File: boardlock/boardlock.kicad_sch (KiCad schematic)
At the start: 15 parts, among them SW1 SW_Push, SW2 SW_Push, U1 ESP32-S3-WROOM-1

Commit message: buttons and stuff
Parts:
- removed C23, C24: 0.1uF, symbol Device:C_Small
- removed D2: CLVBA-FKA-CC1F1L1BB7R3R3D, symbol Device:LED_RABG
- removed R18: 175, symbol Device:R_Small_US
- removed R19, R20: 40, symbol Device:R_Small_US
- removed R21, R22: 10k, symbol Device:R_Small_US
- removed SW1, SW2: SW_Push, symbol Switch:SW_Push
- added TP29, TP30: TestPoint, symbol Connector:TestPoint
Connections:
- net at U1.31 (GPIO38/FSPIWP/SUBSPIWP): now also TP30.1
- net M_BUTTON_INT: now reaches U1.38 (GPIO2/TOUCH2/ADC1_CH1)
- net M_BUTTON_EXT: now reaches U1.39 (GPIO1/TOUCH1/ADC1_CH0)
- net at U1.4 (GPIO4/TOUCH4/ADC1_CH3): now also TP29.1
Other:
- note removed: "assuming using big LED, change pin order if not"
- note removed: "check other circuitry in dev kit schematic"
- note removed: "maybe 100k"
- note removed: "uC dev kit has 2 caps"

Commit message: lab updates
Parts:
- removed TP29, TP30: TestPoint, symbol Connector:TestPoint
- added D3: LED, symbol Device:LED
- added R29: R_US, symbol Device:R_US
- added TP31: TX (backup programming), symbol Connector:TestPoint
- added TP32: RX (backup programming), symbol Connector:TestPoint
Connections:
- net GND: now also D3.1 (K)
- net M_I2S_BCLK: now also U1.24 (GPIO47/SPICLK_P/SUBSPICLK_P_DIFF); no longer U1.8 (GPIO15/U0RTS/ADC2_CH4/XTAL_32K_P)
- net M_I2S_Data_Out: now also U1.26 (GPIO45); no longer U1.22 (GPIO14/TOUCH14/ADC2_CH3/FSPIWP/FSPIDQS/SUBSPIWP)
- net M_I2S_LRC: now also U1.25 (GPIO48/SPICLK_N/SUBSPICLK_N_DIFF); no longer U1.9 (GPIO16/U0CTS/ADC2_CH5/XTAL_32K_N)
- net M_BUTTON_EXT2: now reaches U1.4 (GPIO4/TOUCH4/ADC1_CH3)
- net at U1.36 (U0RXD/GPIO44/CLK_OUT2): now also TP32.1
- net at U1.37 (U0TXD/GPIO43/CLK_OUT1): now also TP31.1
- net M_BUTTON_EXT renamed M_BUTTON_EXT1
- new net: D3.2 (A), R29.2
- new net M_HEARTBEAT: R29.1
- no-connect marks 0 -> 3
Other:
- note added: "35: input only"
- note added: "36: input only"
- note added: "37: input only"
- note added: "38: input only"
- note added: "39: input only"
- note added: "Arrange RGB, I2S, and buttons such that the pins are close to their respective function"
- note added: "figure out what pins can actually be used for stuff"

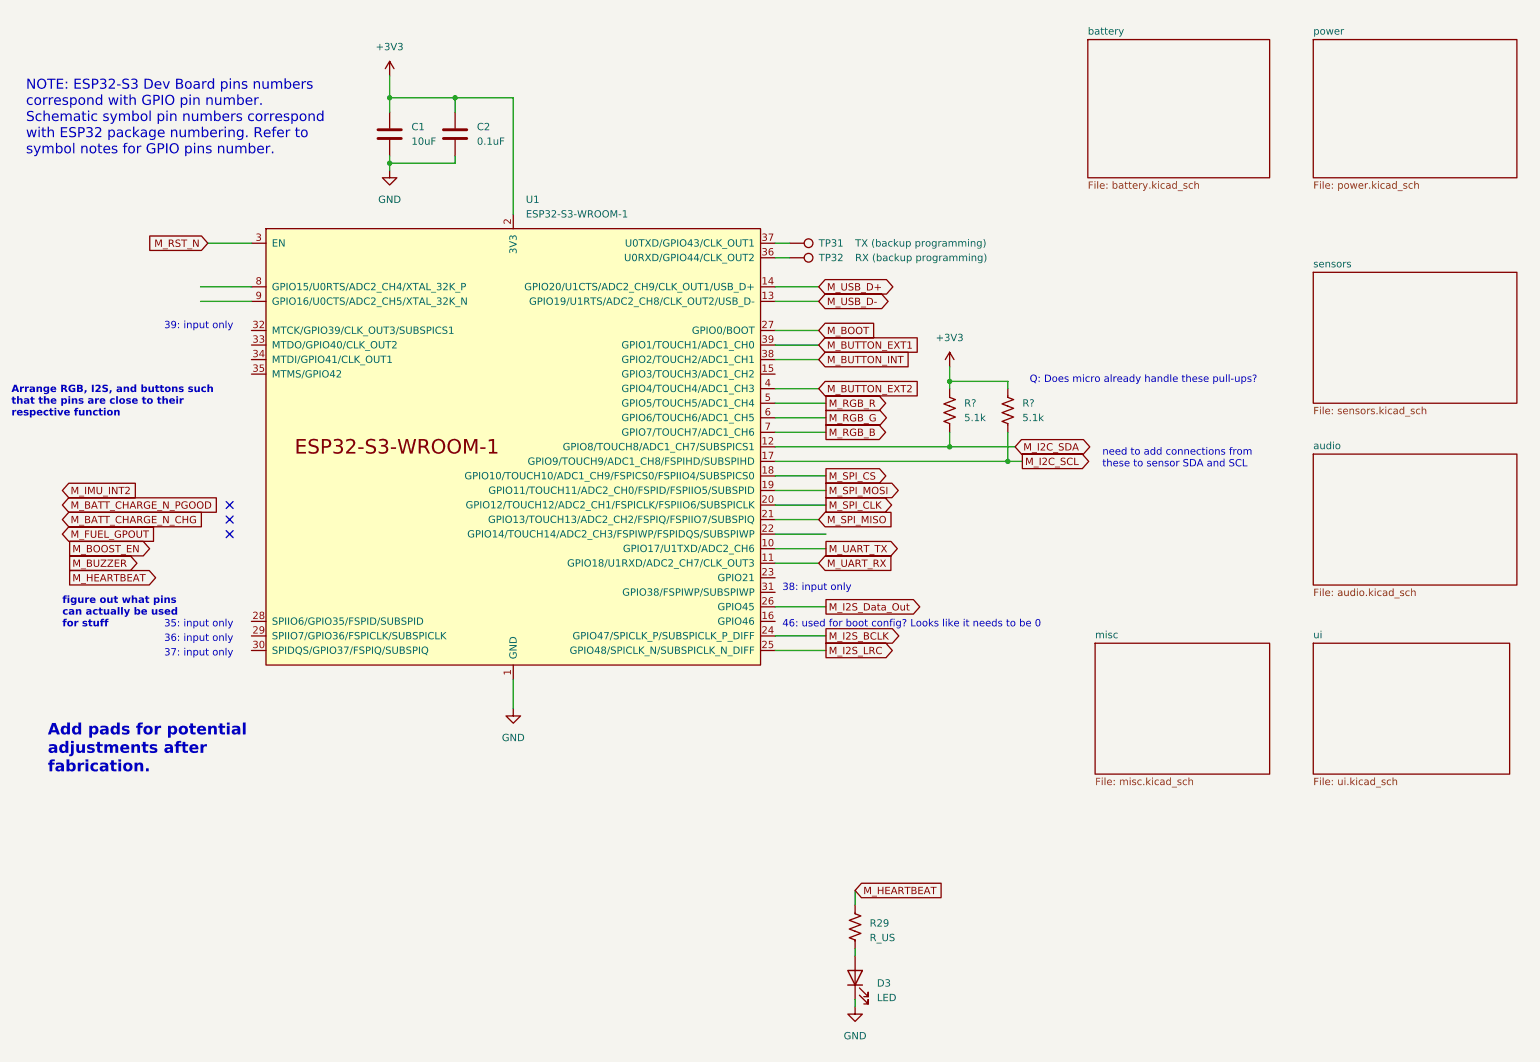
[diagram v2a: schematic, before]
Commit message: added footprints and an LPF to audio
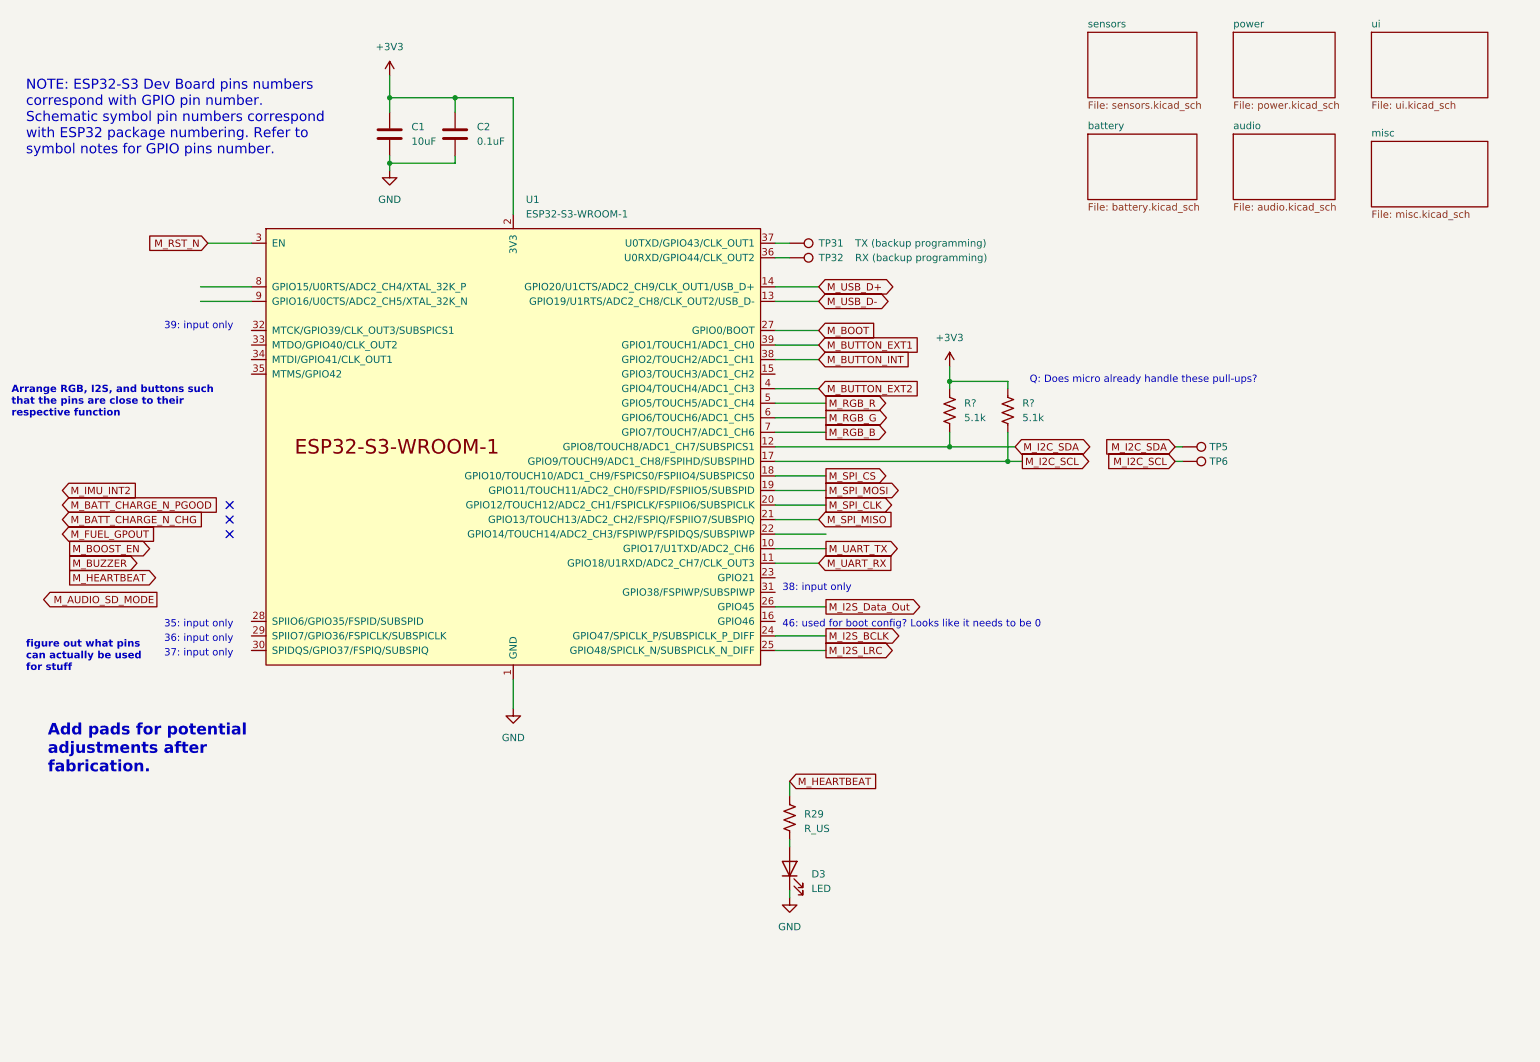
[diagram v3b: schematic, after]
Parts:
- added TP5: I2C_SDA, symbol Connector:TestPoint
- added TP6: I2C_SCL, symbol Connector:TestPoint
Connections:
- net M_I2C_SCL: now also TP6.1
- net M_I2C_SDA: now also TP5.1
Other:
- note removed: "need to add connections from these to sensor SDA and SCL"
- moved on the sheet: D3, R29

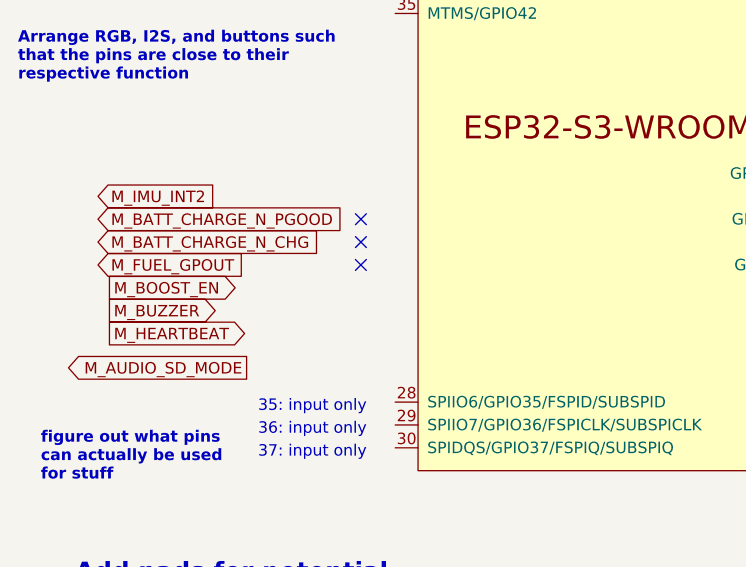
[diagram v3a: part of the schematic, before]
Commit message: note about GPOUT
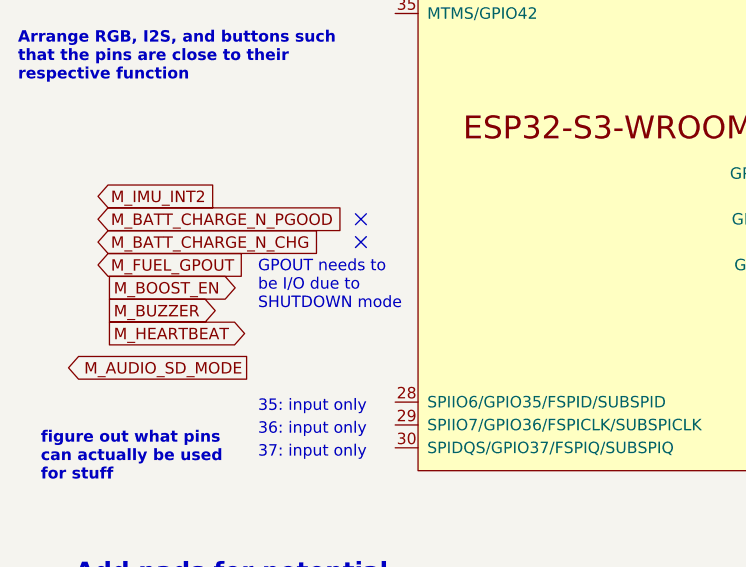
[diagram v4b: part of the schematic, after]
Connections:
- no-connect marks 3 -> 2
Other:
- note added: "GPOUT needs to be I/O due to SHUTDOWN mode"
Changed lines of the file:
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@@
   (no_connect (at 52.07 100.33))
   (no_connect (at 52.07 102.87))
-  (no_connect (at 52.07 105.41))
   (wire (pts (xy 147.32 54.61) (xy 149.86 54.61))
     (stroke (width 0) (type default))
@@
     (effects (font (size 1.27 1.27) bold) (justify left bottom))
   )
+  (text "GPOUT needs to\nbe I/O due to\nSHUTDOWN mode" (at 40.64 110.49 0)
+    (effects (font (size 1.27 1.27)) (justify left bottom))
+  )
   (global_label "M_I2C_SDA" (shape bidirectional) (at 189.23 90.17 0) (fields_autoplaced)

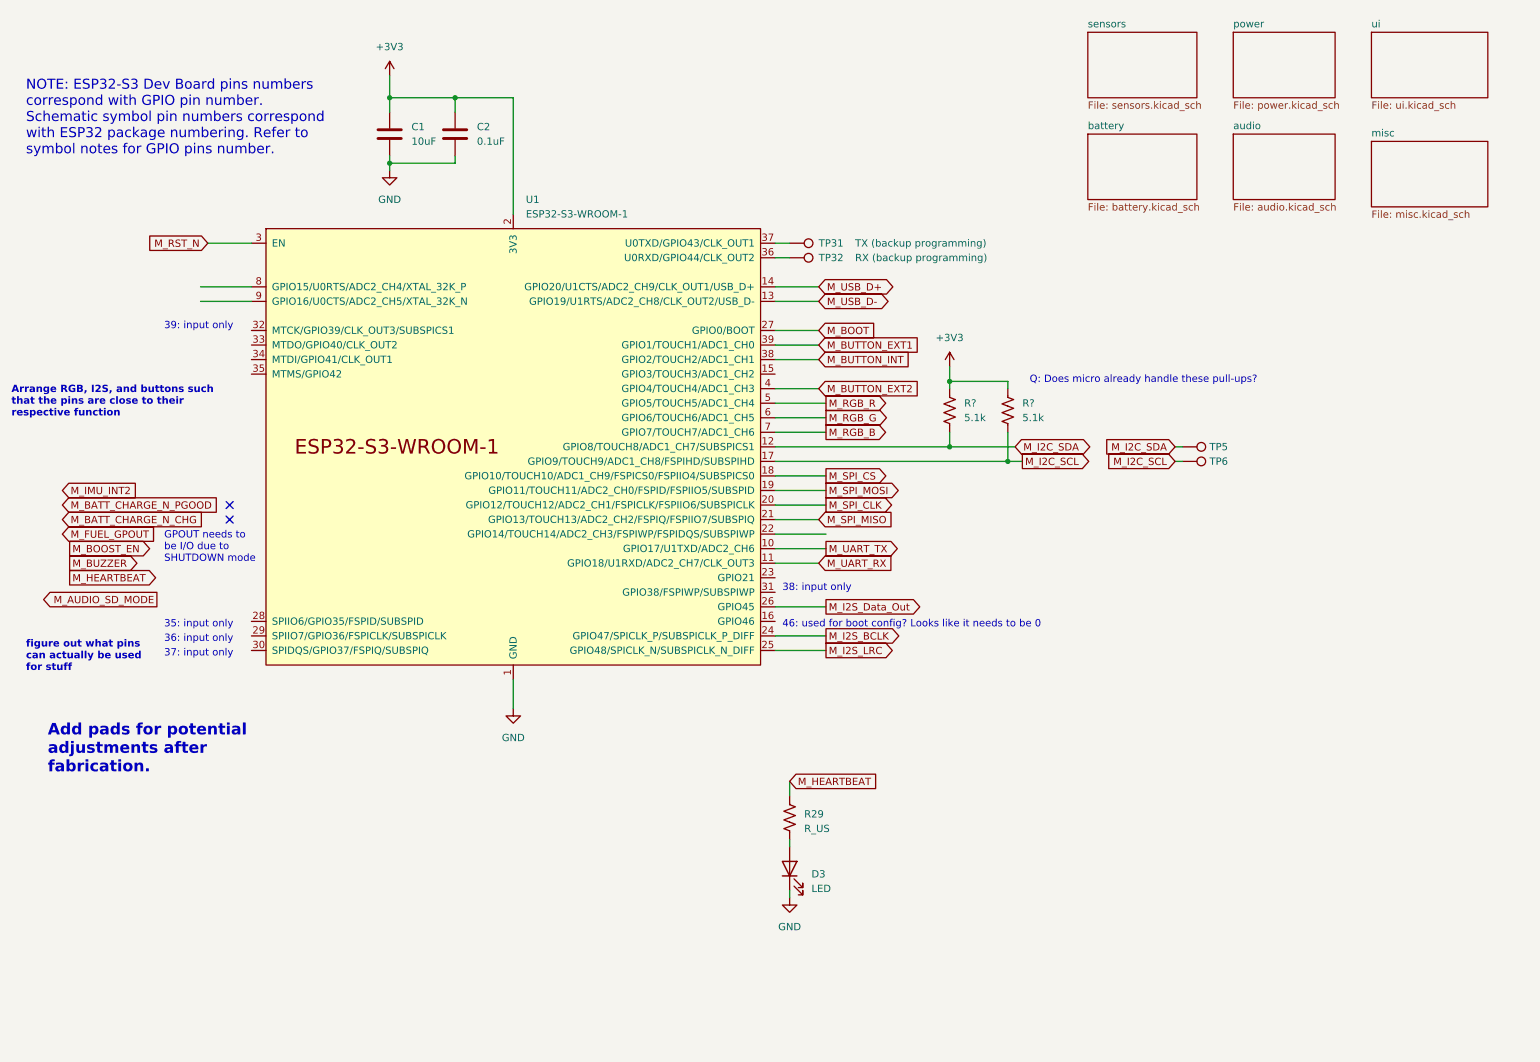
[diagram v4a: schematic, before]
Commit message: allocated pins
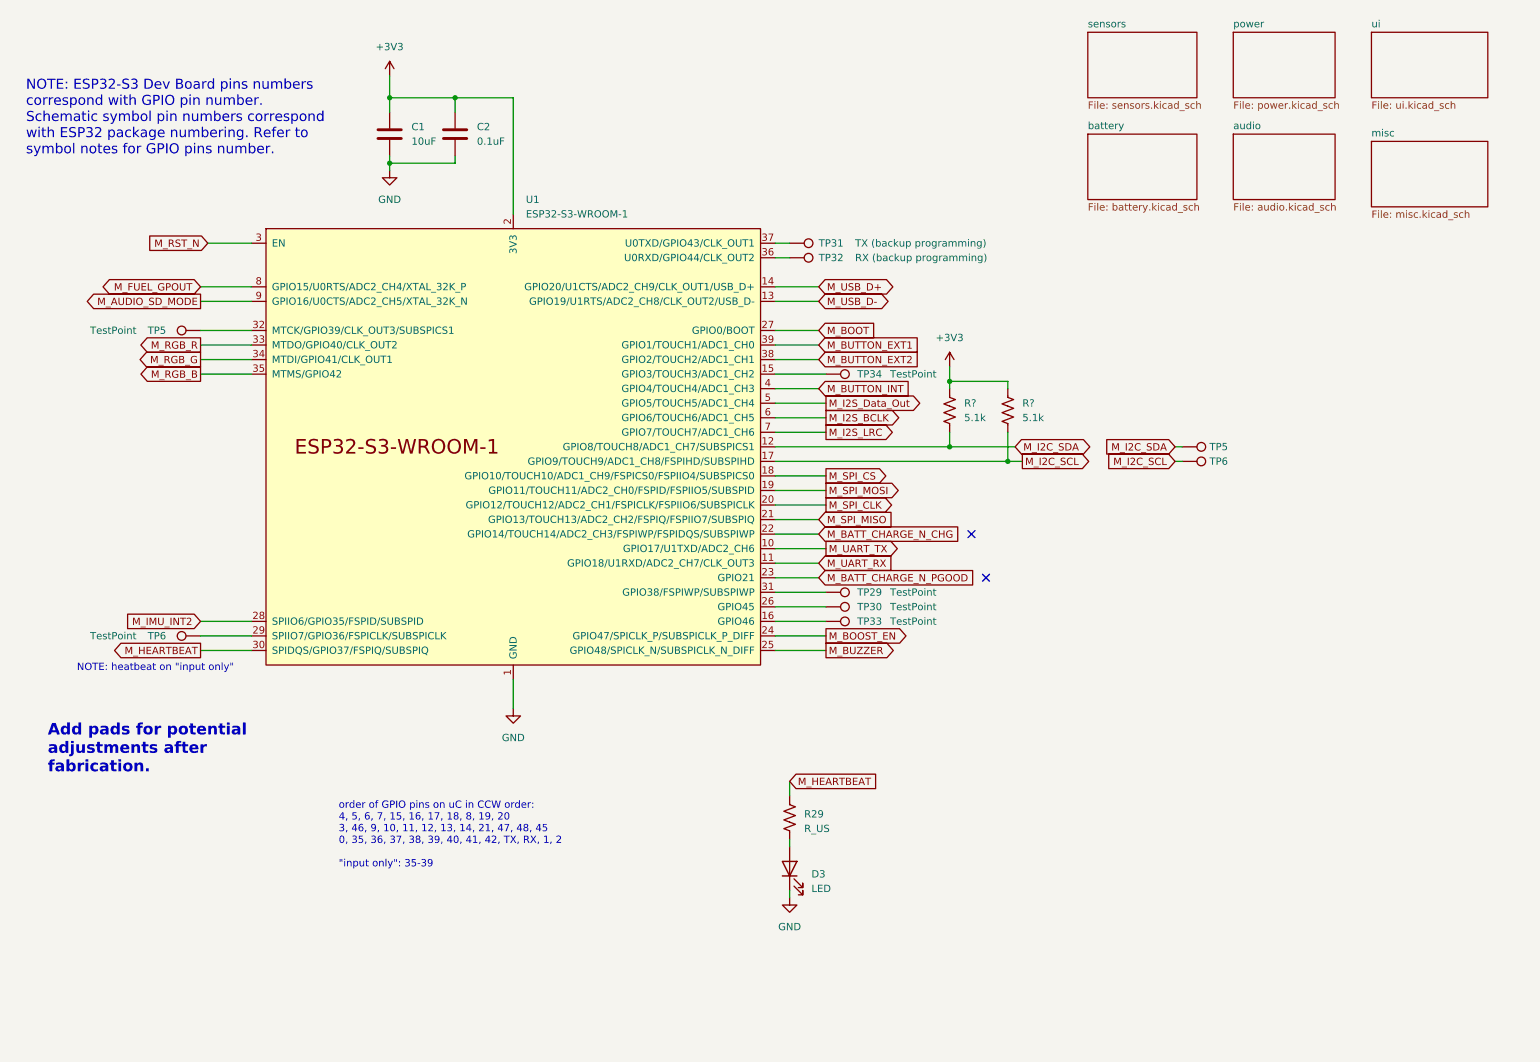
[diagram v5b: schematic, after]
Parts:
- added TP29, TP30, TP33, TP34, TP5, TP6: TestPoint, symbol Connector:TestPoint
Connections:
- net M_AUDIO_SD_MODE: now also U1.9 (GPIO16/U0CTS/ADC2_CH5/XTAL_32K_N)
- net M_BATT_CHARGE_N_CHG: now also U1.22 (GPIO14/TOUCH14/ADC2_CH3/FSPIWP/FSPIDQS/SUBSPIWP)
- net M_BATT_CHARGE_N_PGOOD: now also U1.23 (GPIO21)
- net M_BOOST_EN: now also U1.24 (GPIO47/SPICLK_P/SUBSPICLK_P_DIFF)
- net M_BUTTON_EXT2: now also U1.38 (GPIO2/TOUCH2/ADC1_CH1); no longer U1.4 (GPIO4/TOUCH4/ADC1_CH3)
- net M_BUTTON_INT: now also U1.4 (GPIO4/TOUCH4/ADC1_CH3); no longer U1.38 (GPIO2/TOUCH2/ADC1_CH1)
- net M_BUZZER: now also U1.25 (GPIO48/SPICLK_N/SUBSPICLK_N_DIFF)
- net M_FUEL_GPOUT: now also U1.8 (GPIO15/U0RTS/ADC2_CH4/XTAL_32K_P)
- net M_HEARTBEAT: now also U1.30 (SPIDQS/GPIO37/FSPIQ/SUBSPIQ)
- net M_I2S_BCLK: now also U1.6 (GPIO6/TOUCH6/ADC1_CH5); no longer U1.24 (GPIO47/SPICLK_P/SUBSPICLK_P_DIFF)
- net M_I2S_Data_Out: now also U1.5 (GPIO5/TOUCH5/ADC1_CH4); no longer U1.26 (GPIO45)
- net M_I2S_LRC: now also U1.7 (GPIO7/TOUCH7/ADC1_CH6); no longer U1.25 (GPIO48/SPICLK_N/SUBSPICLK_N_DIFF)
- net M_IMU_INT2: now also U1.28 (SPIIO6/GPIO35/FSPID/SUBSPID)
- net M_RGB_B: now also U1.35 (MTMS/GPIO42); no longer U1.7 (GPIO7/TOUCH7/ADC1_CH6)
- net M_RGB_G: now also U1.34 (MTDI/GPIO41/CLK_OUT1); no longer U1.6 (GPIO6/TOUCH6/ADC1_CH5)
- net M_RGB_R: now also U1.33 (MTDO/GPIO40/CLK_OUT2); no longer U1.5 (GPIO5/TOUCH5/ADC1_CH4)
- net at U1.15 (GPIO3/TOUCH3/ADC1_CH2): now also TP34.1
- net at U1.16 (GPIO46): now also TP33.1
- net at U1.29 (SPIIO7/GPIO36/FSPICLK/SUBSPICLK): now also TP6.1
- net at U1.31 (GPIO38/FSPIWP/SUBSPIWP): now also TP29.1
- net at U1.32 (MTCK/GPIO39/CLK_OUT3/SUBSPICS1): now also TP5.1
- new net: TP30.1, U1.26 (GPIO45)
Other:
- note added: "NOTE: heatbeat on "input only""
- note added: "order of GPIO pins on uC in CCW order: 4, 5, 6, 7, 15, 16, 17, 18, 8, 19, 20 3, 46, 9, 10, 11, 12, 13, 14, 21, 47, 48, 45 0, 35, 36, 37, 38, 39, 40, 41, 42, TX, RX, 1, 2 "input only": 35-39"
- note removed: "35: input only"
- note removed: "36: input only"
- note removed: "37: input only"
- note removed: "38: input only"
- note removed: "39: input only"
- note removed: "46: used for boot config? Looks like it needs to be 0"
- note removed: "Arrange RGB, I2S, and buttons such that the pins are close to their respective function"
- note removed: "GPOUT needs to be I/O due to SHUTDOWN mode"
- note removed: "Q: Does micro already handle these pull-ups?"
- note removed: "figure out what pins can actually be used for stuff"
